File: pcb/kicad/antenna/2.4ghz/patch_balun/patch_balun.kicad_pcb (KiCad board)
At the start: 2 copper layers, 5 parts, among them P1 SMA, P2 Balun

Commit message: Add gerbtool files for new patch tests
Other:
- board text added: "0.1"
- board text removed: "0.2"
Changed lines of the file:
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@@
   (gr_line (start 127 125.2347) (end 170.18 125.2347) (angle 90) (layer Margin) (width 0.2))
   (gr_line (start 127 69.5325) (end 127 125.2347) (angle 90) (layer Margin) (width 0.2))
-  (gr_text 0.2 (at 269.875 193.04) (layer Cmts.User)
+  (gr_text 0.1 (at 269.875 193.04) (layer Cmts.User)
     (effects (font (size 1.5 1.5) (thickness 0.3)))
   )

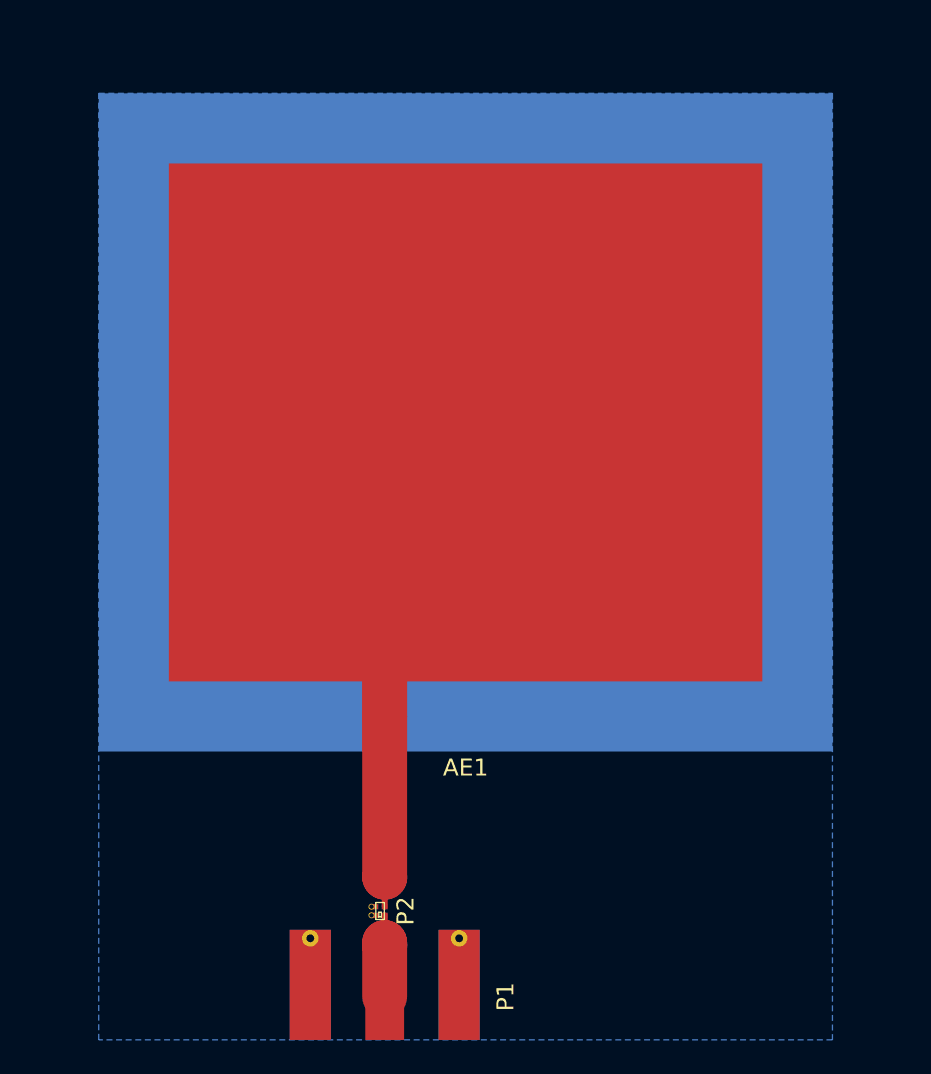
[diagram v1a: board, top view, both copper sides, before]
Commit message: Cleanup balun patch to match regular patch antenna
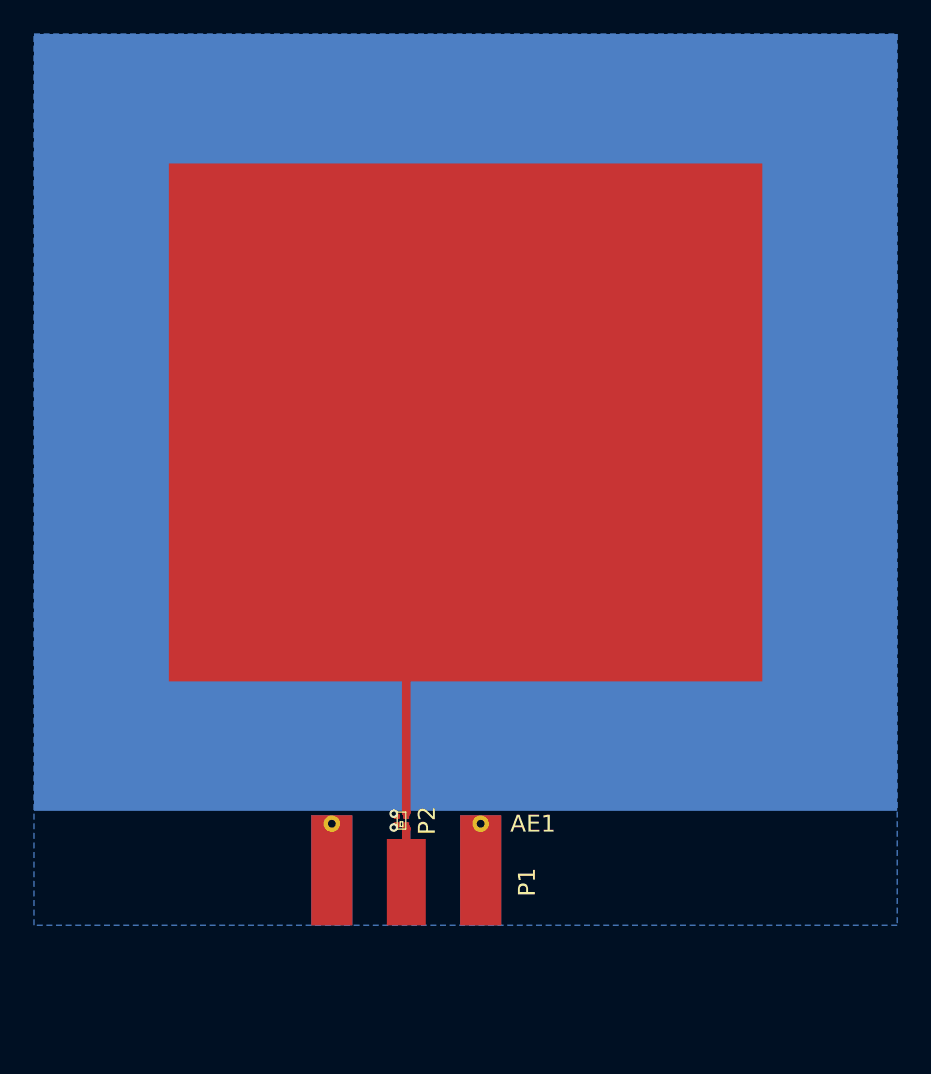
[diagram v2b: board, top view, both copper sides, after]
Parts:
- removed REF** (x2): Via_Stitch_Dia0.356mm_Drill0.254mm, Misc:Via_Stitch_Dia0.356mm_Drill0.254mm
- moved P1 6.86 mm to (145.1, 114.2)
- moved P2 5.47 mm to (144.8, 112.3)
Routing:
- net /SIG_BAL: track 30.5 -> 24.6 mm
- net /SIG_UNBAL: track 5.42 -> 3.38 mm
- net GND: track 0.46 -> 0.49 mm, vias 0 -> 2
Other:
- net class Default: trace_width 2.6416 -> 0.3556; via_dia 0.3556 -> 0.508
- board text added: "0.1.1"
- board text added: "April 5. 2017"
- board text removed: "0.1"
- board text removed: "March 16. 2017"
